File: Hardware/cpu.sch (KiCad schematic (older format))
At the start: 21 parts, among them U13 STM32F411CEU6, Y2 Crystal_Small, Y3 Crystal_GND24

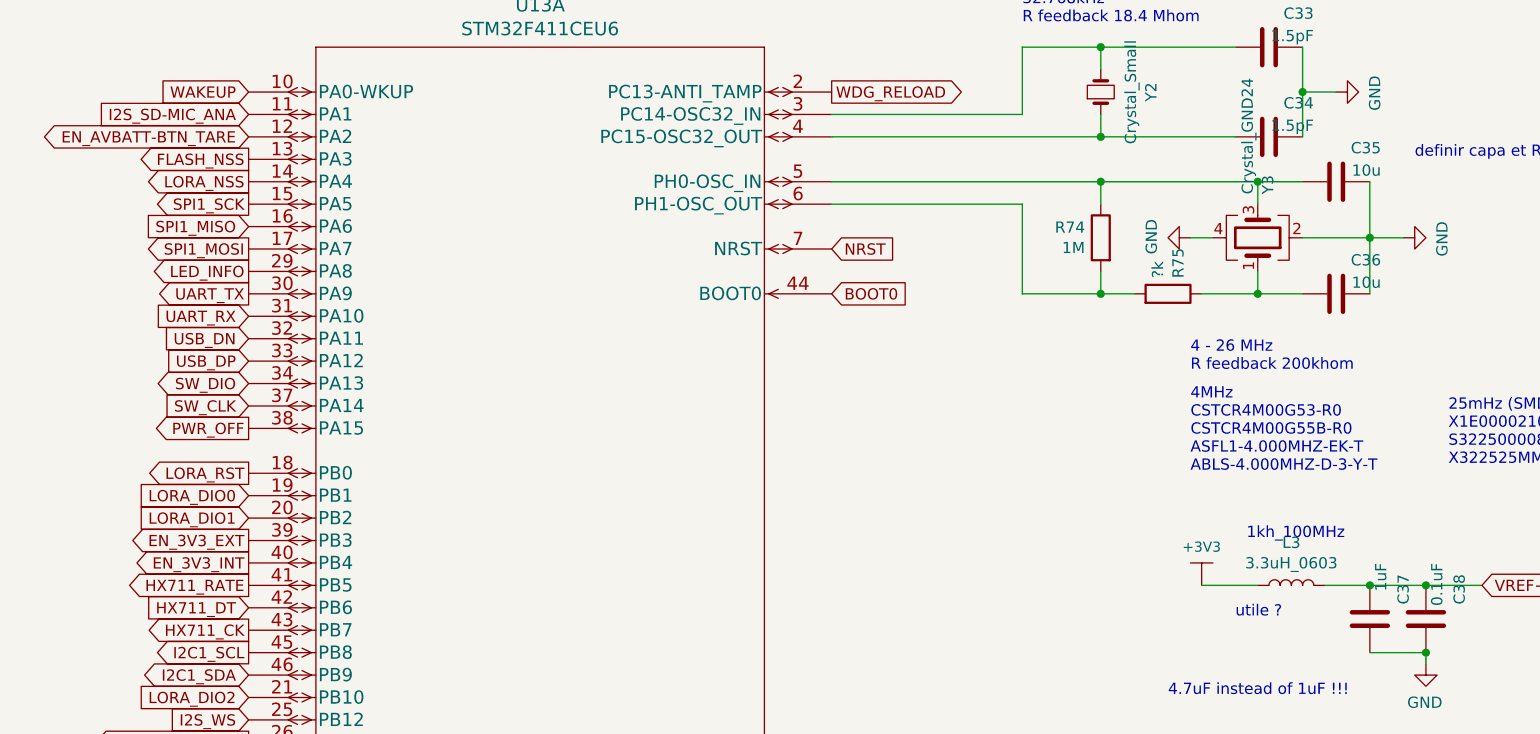
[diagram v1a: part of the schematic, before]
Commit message: Update pcb to v2.1 (Add ldo)
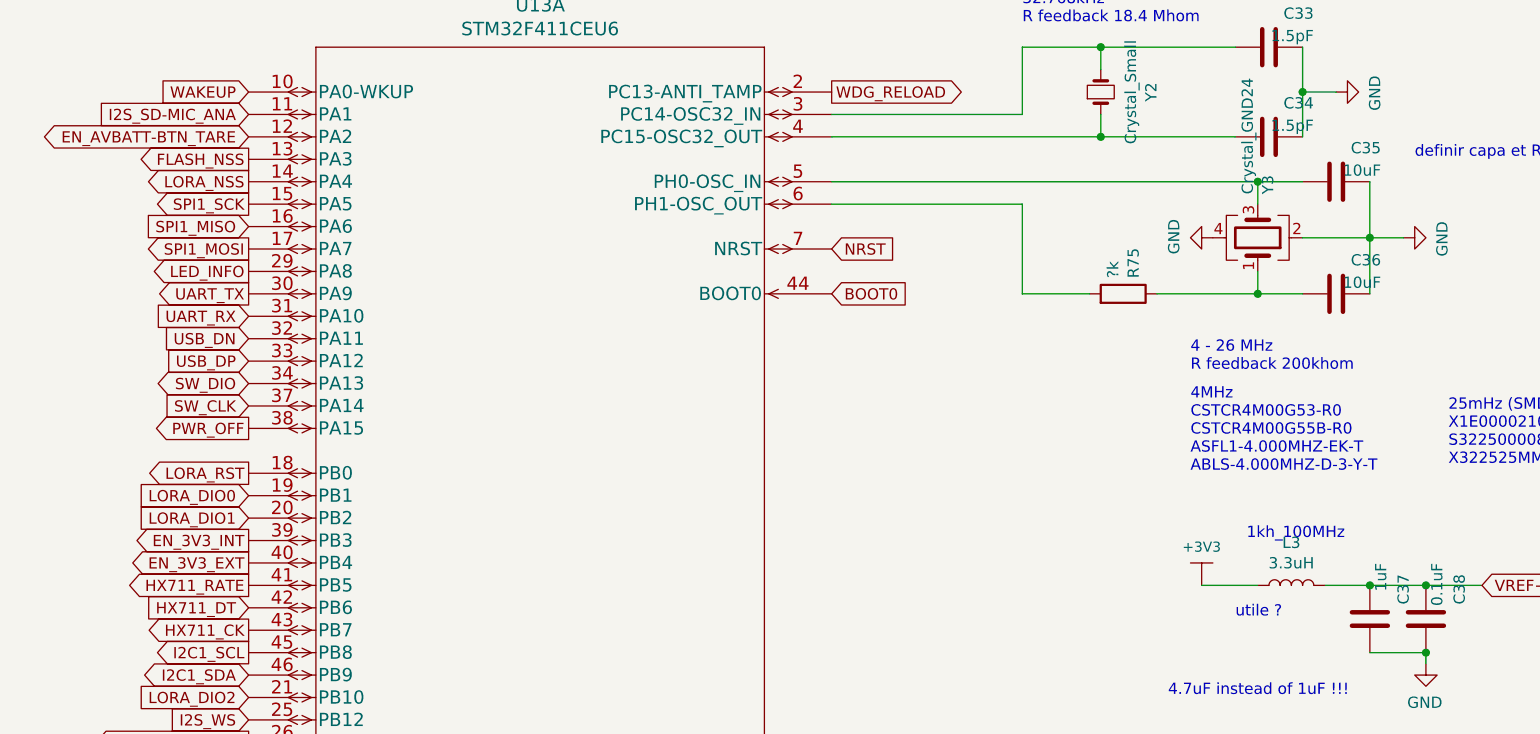
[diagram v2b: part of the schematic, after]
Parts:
- removed R74: 1M, Resistor_SMD:R_0201_0603Metric, symbol Device:R
- C33, C34, C37, C38, C39, C40, C41, C42, C43: Populate (none) -> yes; Size Inch (none) -> 0201; Size Metric (none) -> 0603
- C35, C36: value 10u -> 10uF; Populate (none) -> yes; Size Inch (none) -> 0201; Size Metric (none) -> 0603
- H1, H2, H3, H5: Populate (none) -> no
- L3: value 3.3uH_0603 -> 3.3uH; Populate (none) -> yes
- R75: Populate (none) -> yes; Size Inch (none) -> 0201; Size Metric (none) -> 0603; Tolerance (none) -> 1%
- U13, Y2, Y3: Populate (none) -> yes
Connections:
- net EN_3V3_EXT: now also U13.40 (PB4); no longer U13.39 (PB3)
- net EN_3V3_INT: now also U13.39 (PB3); no longer U13.40 (PB4)
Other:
- moved on the sheet: R75
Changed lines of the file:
@@
 F 2 "MountingHole:MountingHole_2.7mm_M2.5_Pad_Via" H 4050 6700 50  0001 C CNN
 F 3 "~" H 4050 6700 50  0001 C CNN
+F 4 "no" H 4050 6700 50  0001 C CNN "Populate"
 	1    4050 6700
 	1    0    0    -1
@@
 F 2 "MountingHole:MountingHole_2.7mm_M2.5_Pad_Via" H 4050 7000 50  0001 C CNN
 F 3 "~" H 4050 7000 50  0001 C CNN
+F 4 "no" H 4050 7000 50  0001 C CNN "Populate"
 	1    4050 7000
 	-1   0    0    1
@@
 F 2 "Capacitor_SMD:C_0201_0603Metric" H 9888 5000 50  0001 C CNN
 F 3 "~" H 9850 5150 50  0001 C CNN
+F 4 "yes" H 9850 5150 50  0001 C CNN "Populate"
+F 5 "0201" H 9850 5150 50  0001 C CNN "Size Inch"
+F 6 "0603" H 9850 5150 50  0001 C CNN "Size Metric"
 	1    9850 5150
 	0    1    -1   0
@@
 F 2 "EcoApi_pcb:STM32F411CEU6" H 8550 4990 60  0001 C CNN
 F 3 "" H 7750 4750 60  0000 C CNN
+F 4 "yes" H 7750 4750 50  0001 C CNN "Populate"
 	2    7750 4750
 	1    0    0    -1
@@
 F 2 "Capacitor_SMD:C_0201_0603Metric" H 9938 3400 50  0001 C CNN
 F 3 "~" H 9900 3550 50  0001 C CNN
+F 4 "yes" H 9900 3550 50  0001 C CNN "Populate"
+F 5 "0201" H 9900 3550 50  0001 C CNN "Size Inch"
+F 6 "0603" H 9900 3550 50  0001 C CNN "Size Metric"
 	1    9900 3550
 	0    1    -1   0
@@
 F 2 "Capacitor_SMD:C_0201_0603Metric" H 9938 3650 50  0001 C CNN
 F 3 "~" H 9900 3800 50  0001 C CNN
+F 4 "yes" H 9900 3800 50  0001 C CNN "Populate"
+F 5 "0201" H 9900 3800 50  0001 C CNN "Size Inch"
+F 6 "0603" H 9900 3800 50  0001 C CNN "Size Metric"
 	1    9900 3800
 	0    1    -1   0
@@
 F 2 "Capacitor_SMD:C_0201_0603Metric" H 9938 3900 50  0001 C CNN
 F 3 "~" H 9900 4050 50  0001 C CNN
+F 4 "yes" H 9900 4050 50  0001 C CNN "Populate"
+F 5 "0201" H 9900 4050 50  0001 C CNN "Size Inch"
+F 6 "0603" H 9900 4050 50  0001 C CNN "Size Metric"
 	1    9900 4050
 	0    1    -1   0
@@
 F 2 "Capacitor_SMD:C_0201_0603Metric" H 7588 3550 50  0001 C CNN
 F 3 "~" H 7550 3700 50  0001 C CNN
+F 4 "yes" H 7550 3700 50  0001 C CNN "Populate"
+F 5 "0201" H 7550 3700 50  0001 C CNN "Size Inch"
+F 6 "0603" H 7550 3700 50  0001 C CNN "Size Metric"
 	1    7550 3700
 	1    0    0    1
@@
 F 2 "Capacitor_SMD:C_0201_0603Metric" H 7838 3550 50  0001 C CNN
 F 3 "~" H 7800 3700 50  0001 C CNN
+F 4 "yes" H 7800 3700 50  0001 C CNN "Populate"
+F 5 "0201" H 7800 3700 50  0001 C CNN "Size Inch"
+F 6 "0603" H 7800 3700 50  0001 C CNN "Size Metric"
 	1    7800 3700
 	1    0    0    1
@@
 F 2 "Capacitor_SMD:C_0201_0603Metric" H 9938 3150 50  0001 C CNN
 F 3 "~" H 9900 3300 50  0001 C CNN
+F 4 "yes" H 9900 3300 50  0001 C CNN "Populate"
+F 5 "0201" H 9900 3300 50  0001 C CNN "Size Inch"
+F 6 "0603" H 9900 3300 50  0001 C CNN "Size Metric"
 	1    9900 3300
 	0    1    -1   0
@@
 Text GLabel 2550 4150 0    50   Input ~ 0
 I2S_WS
-Text GLabel 2550 3350 0    50   Output ~ 0
+Text GLabel 2550 3450 0    50   Output ~ 0
 EN_3V3_EXT
 Text GLabel 2550 3550 0    50   Output ~ 0
 HX711_RATE
-Text GLabel 2550 3450 0    50   Output ~ 0
+Text GLabel 2550 3350 0    50   Output ~ 0
 EN_3V3_INT
 Text GLabel 2550 3750 0    50   Output ~ 0
@@
 L power:GND #PWR?
 U 1 1 623CA95E
-P 6750 2000
+P 6850 2000
 AR Path="/623CA95E" Ref="#PWR?"  Part="1"
 AR Path="/62B8145A/623CA95E" Ref="#PWR0181"  Part="1"
-F 0 "#PWR0181" H 6750 1750 50  0001 C CNN
-F 1 "GND" H 6755 1827 50  0000 C CNN
-F 2 "" H 6750 2000 50  0001 C CNN
-F 3 "" H 6750 2000 50  0001 C CNN
-	1    6750 2000
+F 0 "#PWR0181" H 6850 1750 50  0001 C CNN
+F 1 "GND" H 6855 1827 50  0000 C CNN
+F 2 "" H 6850 2000 50  0001 C CNN
+F 3 "" H 6850 2000 50  0001 C CNN
+	1    6850 2000
 	0    1    -1   0
 $EndComp
@@
 F 2 "EcoApi_pcb:X322525MMB4SI" H 7050 2000 50  0001 C CNN
 F 3 "~" H 7050 2000 50  0001 C CNN
+F 4 "yes" H 7050 2000 50  0001 C CNN "Populate"
 	1    7050 2000
 	0    1    -1   0
@@
 AR Path="/62B8145A/623CA94A" Ref="C35"  Part="1"
 F 0 "C35" V 7550 1550 50  0000 L CNN
-F 1 "10u" V 7450 1550 50  0000 L CNN
+F 1 "10uF" V 7450 1550 50  0000 L CNN
 F 2 "Capacitor_SMD:C_0201_0603Metric" H 7438 1600 50  0001 C CNN
 F 3 "~" H 7400 1750 50  0001 C CNN
+F 4 "yes" H 7400 1750 50  0001 C CNN "Populate"
+F 5 "0201" H 7400 1750 50  0001 C CNN "Size Inch"
+F 6 "0603" H 7400 1750 50  0001 C CNN "Size Metric"
 	1    7400 1750
 	0    -1   -1   0
@@
 AR Path="/62B8145A/623CA944" Ref="C36"  Part="1"
 F 0 "C36" V 7550 2050 50  0000 L CNN
-F 1 "10u" V 7450 2050 50  0000 L CNN
+F 1 "10uF" V 7450 2050 50  0000 L CNN
 F 2 "Capacitor_SMD:C_0201_0603Metric" H 7438 2100 50  0001 C CNN
 F 3 "~" H 7400 2250 50  0001 C CNN
+F 4 "yes" H 7400 2250 50  0001 C CNN "Populate"
+F 5 "0201" H 7400 2250 50  0001 C CNN "Size Inch"
+F 6 "0603" H 7400 2250 50  0001 C CNN "Size Metric"
 	1    7400 2250
 	0    -1   -1   0
@@
 L Device:R R?
 U 1 1 623CA93C
-P 6650 2250
+P 6450 2250
 AR Path="/623CA93C" Ref="R?"  Part="1"
 AR Path="/62B8145A/623CA93C" Ref="R75"  Part="1"
-F 0 "R75" H 6720 2296 50  0000 L CNN
-F 1 "?k" H 6720 2205 50  0000 L CNN
-F 2 "Resistor_SMD:R_0201_0603Metric" V 6580 2250 50  0001 C CNN
-F 3 "~" H 6650 2250 50  0001 C CNN
-	1    6650 2250
-	0    1    -1   0
-$EndComp
-$Comp
-L Device:R R?
-U 1 1 623CA936
-P 6350 2000
-AR Path="/623CA936" Ref="R?"  Part="1"
-AR Path="/62B8145A/623CA936" Ref="R74"  Part="1"
-F 0 "R74" H 6420 2046 50  0000 L CNN
-F 1 "1M" H 6420 1955 50  0000 L CNN
-F 2 "Resistor_SMD:R_0201_0603Metric" V 6280 2000 50  0001 C CNN
-F 3 "~" H 6350 2000 50  0001 C CNN
-	1    6350 2000
-	-1   0    0    -1
+F 0 "R75" H 6520 2296 50  0000 L CNN
+F 1 "?k" H 6520 2205 50  0000 L CNN
+F 2 "Resistor_SMD:R_0201_0603Metric" V 6380 2250 50  0001 C CNN
+F 3 "~" H 6450 2250 50  0001 C CNN
+F 4 "yes" H 6450 2250 50  0001 C CNN "Populate"
+F 5 "0201" H 6450 2250 50  0001 C CNN "Size Inch"
+F 6 "0603" H 6450 2250 50  0001 C CNN "Size Metric"
+F 7 "1%" H 6450 2250 50  0001 C CNN "Tolerance"
+	1    6450 2250
+	0    1    -1   0
 $EndComp
 Wire Wire Line
@@
 Wire Wire Line
 	7250 2250 7050 2250
-Wire Wire Line
-	6850 2000 6750 2000
 Wire Wire Line
 	7700 2000 7550 2000
@@
 F 2 "EcoApi_pcb:XTAL_ABS07-120-32.768KHZ-T" H 6350 1350 50  0001 C CNN
 F 3 "~" H 6350 1350 50  0001 C CNN
+F 4 "yes" H 6350 1350 50  0001 C CNN "Populate"
 	1    6350 1350
 	0    1    -1   0
@@
 F 2 "EcoApi_pcb:STM32F411CEU6" H 3350 1590 60  0001 C CNN
 F 3 "" H 2550 1350 60  0000 C CNN
+F 4 "yes" H 2550 1350 50  0001 C CNN "Populate"
 	1    2550 1350
 	1    0    0    -1
@@
 Wire Wire Line
 	6000 1850 5150 1850
-Wire Wire Line
-	5150 1750 6350 1750
-Wire Wire Line
-	6000 2250 6350 2250
-Wire Wire Line
-	6350 1850 6350 1750
-Wire Wire Line
-	6350 2150 6350 2250
-Wire Wire Line
-	6500 2250 6350 2250
-Connection ~ 6350 2250
-Wire Wire Line
-	7050 1750 6350 1750
 Connection ~ 7050 1750
-Connection ~ 6350 1750
-Wire Wire Line
-	6800 2250 7050 2250
-Connection ~ 7050 2250
 Wire Wire Line
 	7250 1350 7250 1550
@@
 F 2 "Capacitor_SMD:C_0201_0603Metric" H 7138 1400 50  0001 C CNN
 F 3 "~" H 7100 1550 50  0001 C CNN
+F 4 "yes" H 7100 1550 50  0001 C CNN "Populate"
+F 5 "0201" H 7100 1550 50  0001 C CNN "Size Inch"
+F 6 "0603" H 7100 1550 50  0001 C CNN "Size Metric"
 	1    7100 1550
 	0    -1   -1   0
@@
 F 2 "Capacitor_SMD:C_0201_0603Metric" H 7138 1000 50  0001 C CNN
 F 3 "~" H 7100 1150 50  0001 C CNN
+F 4 "yes" H 7100 1150 50  0001 C CNN "Populate"
+F 5 "0201" H 7100 1150 50  0001 C CNN "Size Inch"
+F 6 "0603" H 7100 1150 50  0001 C CNN "Size Metric"
 	1    7100 1150
 	0    -1   -1   0
@@
 F 2 "MountingHole:MountingHole_2.7mm_M2.5_Pad_Via" H 3450 6700 50  0001 C CNN
 F 3 "~" H 3450 6700 50  0001 C CNN
+F 4 "no" H 3450 6700 50  0001 C CNN "Populate"
 	1    3450 6700
 	1    0    0    -1
@@
 F 2 "MountingHole:MountingHole_2.7mm_M2.5_Pad_Via" H 3750 6700 50  0001 C CNN
 F 3 "~" H 3750 6700 50  0001 C CNN
+F 4 "no" H 3750 6700 50  0001 C CNN "Populate"
 	1    3750 6700
 	1    0    0    -1
@@
 AR Path="/62B8145A/63D4FB09" Ref="L3"  Part="1"
 F 0 "L3" V 7390 3550 50  0000 C CNN
-F 1 "3.3uH_0603" V 7299 3550 50  0000 C CNN
+F 1 "3.3uH" V 7299 3550 50  0000 C CNN
 F 2 "Inductor_SMD:L_0402_1005Metric" H 7200 3550 50  0001 C CNN
 F 3 "~" H 7200 3550 50  0001 C CNN
+F 4 "yes" H 7200 3550 50  0001 C CNN "Populate"
 	1    7200 3550
 	0    -1   -1   0
@@
 	7350 3550 7550 3550
 Connection ~ 7550 3550
+Wire Wire Line
+	5150 1750 7050 1750
+Wire Wire Line
+	7050 2250 6600 2250
+Connection ~ 7050 2250
+Wire Wire Line
+	6000 2250 6300 2250
 $EndSCHEMATC
